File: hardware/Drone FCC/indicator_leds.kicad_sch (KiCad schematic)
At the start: 46 parts, among them Q2 2N7002, Q3 2N7002, Q4 2N7002, Q5 2N7002, Q6 2N7002, Q7 2N7002, Q8 2N7002, Q9 2N7002, SW2 SW_MEC_5E, SW3 SW_MEC_5E

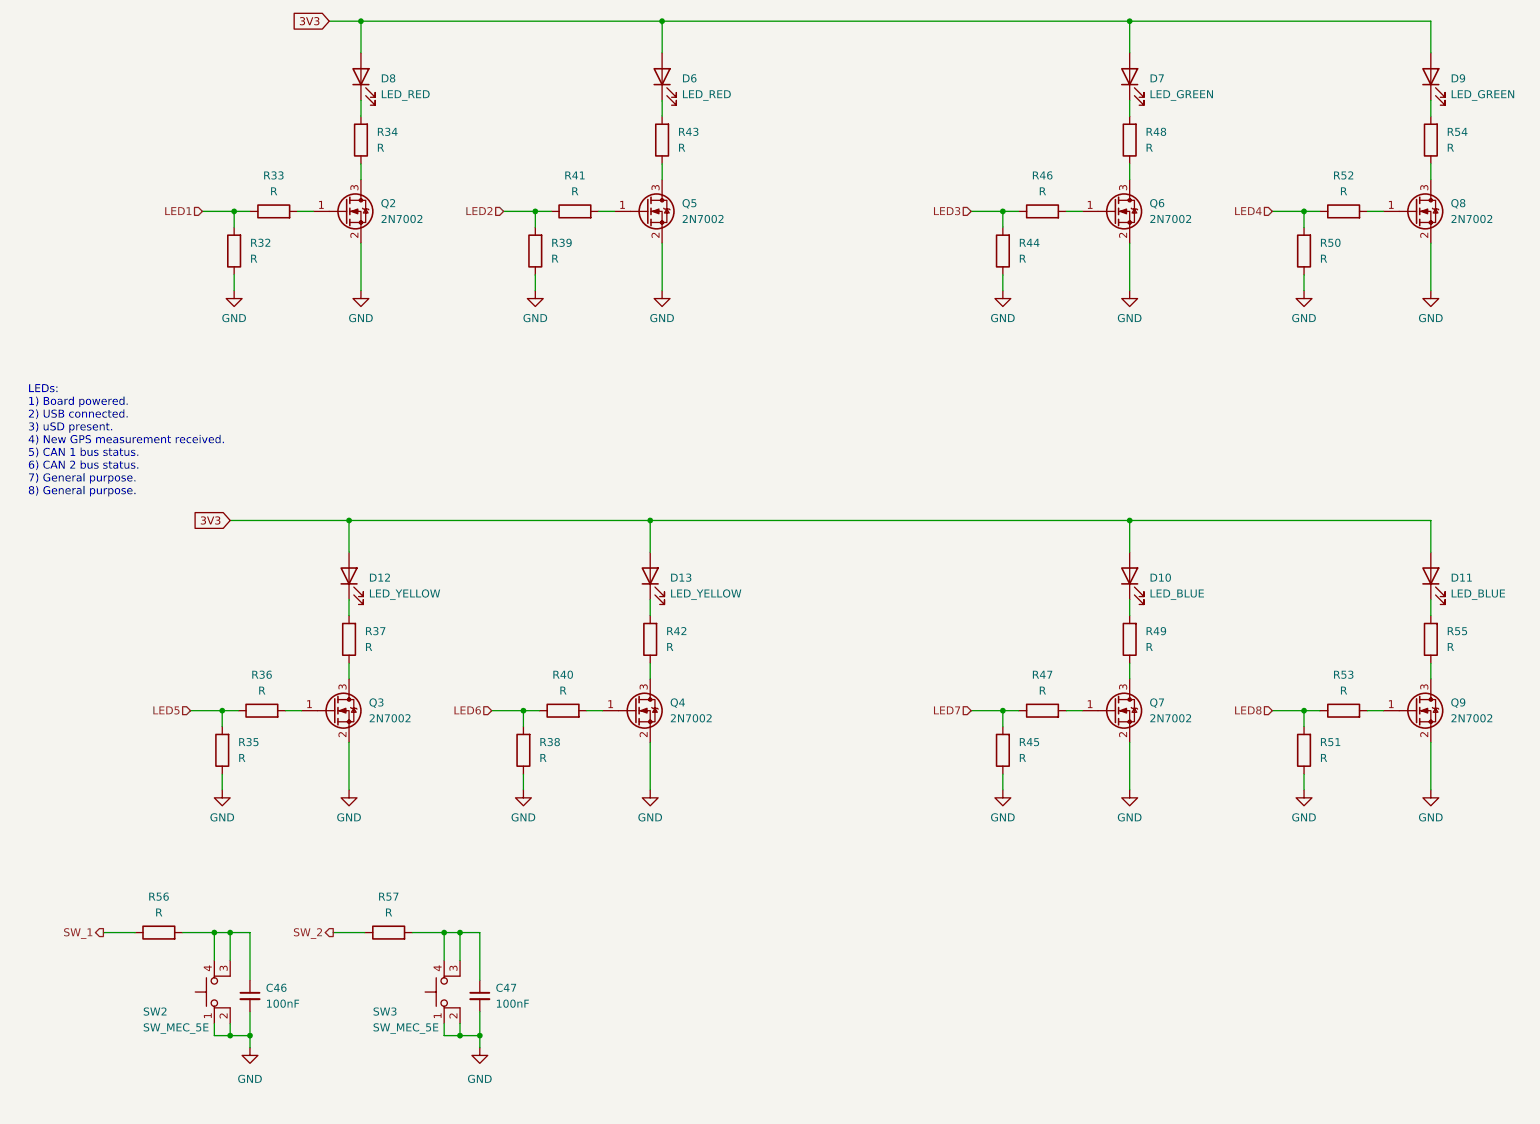
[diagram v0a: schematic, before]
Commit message: re enumeration of components
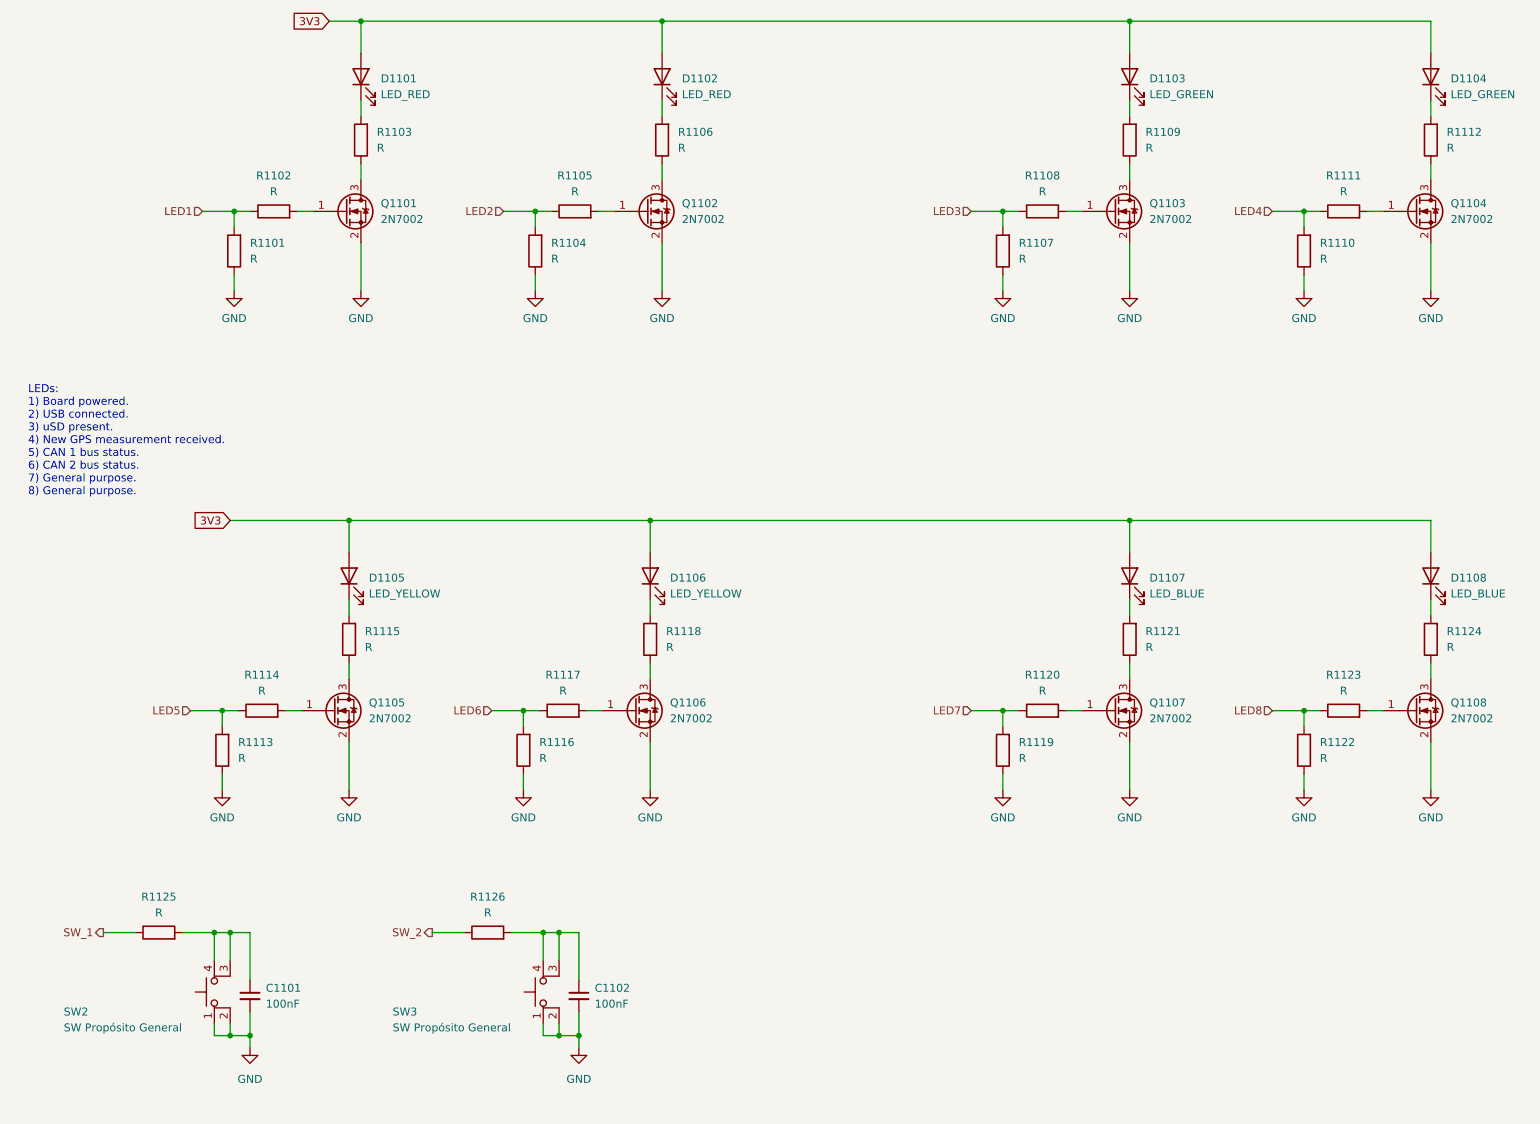
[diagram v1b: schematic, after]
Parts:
- SW2, SW3: value SW_MEC_5E -> SW Propósito General
- renumbered C46 to C1101, C47 to C1102, D8 to D1101, D6 to D1102, D7 to D1103, D9 to D1104, D12 to D1105, D13 to D1106, D10 to D1107, D11 to D1108, Q2 to Q1101, Q5 to Q1102, Q6 to Q1103, Q8 to Q1104, Q3 to Q1105, Q4 to Q1106, Q7 to Q1107, Q9 to Q1108, R32 to R1101, R33 to R1102, R34 to R1103, R39 to R1104, R41 to R1105, R43 to R1106, R44 to R1107, R46 to R1108, R48 to R1109, R50 to R1110, R52 to R1111, R54 to R1112, R35 to R1113, R36 to R1114, R37 to R1115, R38 to R1116, R40 to R1117, R42 to R1118, R45 to R1119, R47 to R1120, R49 to R1121, R51 to R1122, R53 to R1123, R55 to R1124, R56 to R1125, R57 to R1126
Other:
- moved on the sheet: C1102, R1126, SW3

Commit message: start routing
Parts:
- removed SW2, SW3: SW Propósito General, Button_Switch_SMD:SW_SPST_TL3305A, symbol Switch:SW_MEC_5E
- added SW1101, SW1102: SW Propósito General, Button_Switch_SMD:SW_SPST_TL3305A, symbol Switch:SW_Push
- C1101, C1102: footprint (none) -> Capacitor_SMD:C_0402_1005Metric_Pad0.74x0.62mm_HandSolder
- R1101, R1102, R1104, R1105, R1107, R1108, R1110, R1111, R1113, R1114, R1116, R1117, R1119, R1120, R1122, R1123, R1125, R1126: footprint (none) -> Resistor_SMD:R_0402_1005Metric_Pad0.72x0.64mm_HandSolder
- R1103, R1106, R1109, R1112, R1115, R1118, R1121, R1124: footprint (none) -> Resistor_SMD:R_0805_2012Metric_Pad1.20x1.40mm_HandSolder
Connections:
- net GND: now also SW1101.1, SW1102.1
- net at C1102.1, R1126.2: now also SW1102.2
- net at C1101.1, R1125.2: now also SW1101.2

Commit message: add 3D models to footprints
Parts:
- removed SW1101, SW1102: SW Propósito General, Button_Switch_SMD:SW_SPST_TL3305A, symbol Switch:SW_Push
- added SW1101, SW1102: SW Proposito General, TL3305AF160QG:SW_TL3305AF160QG, symbol Switch:SW_MEC_5E
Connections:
- net GND: now also SW1101.1, SW1101.2, SW1102.1, SW1102.2
- net at C1102.1, R1126.2: now also SW1102.3 (K), SW1102.4 (A)
- net at C1101.1, R1125.2: now also SW1101.3 (K), SW1101.4 (A)
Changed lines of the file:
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@@
   (junction (at 49.53 47.625) (diameter 0) (color 0 0 0 0)
   )
+  (junction (at 99.06 165.735) (diameter 0) (color 0 0 0 0)
+  )
   (junction (at 46.355 163.195) (diameter 0) (color 0 0 0 0)
   )
@@
   (junction (at 99.06 163.195) (diameter 0) (color 0 0 0 0)
   )
+  (junction (at 46.355 165.735) (diameter 0) (color 0 0 0 0)
+  )
+  (junction (at 46.355 179.705) (diameter 0) (color 0 0 0 0)
+  )
   (junction (at 220.98 47.625) (diameter 0) (color 0 0 0 0)
   )
@@
   (junction (at 67.945 97.155) (diameter 0) (color 0 0 0 0)
   )
+  (junction (at 99.06 179.705) (diameter 0) (color 0 0 0 0)
+  )
   (junction (at 172.72 127.635) (diameter 0) (color 0 0 0 0)
   )
@@
     (stroke (width 0) (type default) (color 0 0 0 0))
   )
+  (wire (pts (xy 96.52 179.705) (xy 99.06 179.705))
+    (stroke (width 0) (type default) (color 0 0 0 0))
+  )
   (wire (pts (xy 182.88 47.625) (xy 185.42 47.625))
     (stroke (width 0) (type default) (color 0 0 0 0))
@@
     (stroke (width 0) (type default) (color 0 0 0 0))
   )
+  (wire (pts (xy 96.52 177.8) (xy 96.52 179.705))
+    (stroke (width 0) (type default) (color 0 0 0 0))
+  )
   (wire (pts (xy 193.04 17.145) (xy 193.04 22.225))
     (stroke (width 0) (type default) (color 0 0 0 0))
@@
     (stroke (width 0) (type default) (color 0 0 0 0))
   )
+  (wire (pts (xy 43.815 165.735) (xy 46.355 165.735))
+    (stroke (width 0) (type default) (color 0 0 0 0))
+  )
+  (wire (pts (xy 99.06 163.195) (xy 99.06 165.735))
+    (stroke (width 0) (type default) (color 0 0 0 0))
+  )
   (wire (pts (xy 67.945 97.155) (xy 67.945 102.235))
     (stroke (width 0) (type default) (color 0 0 0 0))
@@
     (stroke (width 0) (type default) (color 0 0 0 0))
   )
+  (wire (pts (xy 46.355 165.735) (xy 46.355 167.64))
+    (stroke (width 0) (type default) (color 0 0 0 0))
+  )
   (wire (pts (xy 57.785 127.635) (xy 60.325 127.635))
     (stroke (width 0) (type default) (color 0 0 0 0))
@@
     (stroke (width 0) (type default) (color 0 0 0 0))
   )
+  (wire (pts (xy 43.815 177.8) (xy 43.815 179.705))
+    (stroke (width 0) (type default) (color 0 0 0 0))
+  )
   (wire (pts (xy 116.205 132.715) (xy 116.205 140.335))
     (stroke (width 0) (type default) (color 0 0 0 0))
@@
     (stroke (width 0) (type default) (color 0 0 0 0))
   )
+  (wire (pts (xy 96.52 167.64) (xy 96.52 165.735))
+    (stroke (width 0) (type default) (color 0 0 0 0))
+  )
   (wire (pts (xy 67.945 120.015) (xy 67.945 122.555))
     (stroke (width 0) (type default) (color 0 0 0 0))
@@
     (stroke (width 0) (type default) (color 0 0 0 0))
   )
+  (wire (pts (xy 96.52 165.735) (xy 99.06 165.735))
+    (stroke (width 0) (type default) (color 0 0 0 0))
+  )
   (wire (pts (xy 118.11 40.005) (xy 118.11 42.545))
     (stroke (width 0) (type default) (color 0 0 0 0))
@@
     (stroke (width 0) (type default) (color 0 0 0 0))
   )
+  (wire (pts (xy 43.815 167.64) (xy 43.815 165.735))
+    (stroke (width 0) (type default) (color 0 0 0 0))
+  )
   (wire (pts (xy 167.64 127.635) (xy 172.72 127.635))
     (stroke (width 0) (type default) (color 0 0 0 0))
@@
     (stroke (width 0) (type default) (color 0 0 0 0))
   )
+  (wire (pts (xy 43.815 179.705) (xy 46.355 179.705))
+    (stroke (width 0) (type default) (color 0 0 0 0))
+  )
   (wire (pts (xy 118.11 52.705) (xy 118.11 60.325))
     (stroke (width 0) (type default) (color 0 0 0 0))
@@
     (stroke (width 0) (type default) (color 0 0 0 0))
   )
+  (wire (pts (xy 99.06 165.735) (xy 99.06 167.64))
+    (stroke (width 0) (type default) (color 0 0 0 0))
+  )
   (wire (pts (xy 52.07 175.895) (xy 52.07 179.705))
     (stroke (width 0) (type default) (color 0 0 0 0))
@@
     (stroke (width 0) (type default) (color 0 0 0 0))
   )
-  (wire (pts (xy 46.355 163.195) (xy 46.355 167.64))
+  (wire (pts (xy 46.355 163.195) (xy 46.355 165.735))
     (stroke (width 0) (type default) (color 0 0 0 0))
   )
@@
   )
   (wire (pts (xy 241.3 109.855) (xy 241.3 112.395))
-    (stroke (width 0) (type default) (color 0 0 0 0))
-  )
-  (wire (pts (xy 99.06 163.195) (xy 99.06 167.64))
     (stroke (width 0) (type default) (color 0 0 0 0))
   )
@@
     (pin "2")
   )
-  (symbol (lib_id "Switch:SW_Push") (at 46.355 172.72 90) (unit 1)
-    (in_bom yes) (on_board yes)
-    (property "Reference" "SW1101" (id 0) (at 34.925 171.45 90)
-      (effects (font (size 1.27 1.27)) (justify right))
-    )
-    (property "Value" "SW Propósito General" (id 1) (at 21.59 173.99 90)
-      (effects (font (size 1.27 1.27)) (justify right))
-    )
-    (property "Footprint" "Button_Switch_SMD:SW_SPST_TL3305A" (id 2) (at 41.275 172.72 0)
-      (effects (font (size 1.27 1.27)) hide)
-    )
-    (property "Datasheet" "~" (id 3) (at 41.275 172.72 0)
-      (effects (font (size 1.27 1.27)) hide)
-    )
-    (pin "1")
-    (pin "2")
-  )
   (symbol (lib_id "Device:R") (at 241.3 36.195 180) (unit 1)
     (in_bom yes) (on_board yes) (fields_autoplaced)
@@
     (pin "1")
   )
+  (symbol (lib_id "Switch:SW_MEC_5E") (at 46.355 172.72 90) (unit 1)
+    (in_bom yes) (on_board yes)
+    (property "Reference" "SW1101" (id 0) (at 32.385 172.085 90)
+      (effects (font (size 1.27 1.27)) (justify right))
+    )
+    (property "Value" "SW Proposito General" (id 1) (at 19.05 174.625 90)
+      (effects (font (size 1.27 1.27)) (justify right))
+    )
+    (property "Footprint" "TL3305AF160QG:SW_TL3305AF160QG" (id 2) (at 38.735 172.72 0)
+      (effects (font (size 1.27 1.27)) hide)
+    )
+    (property "Datasheet" "http://www.apem.com/int/index.php?controller=attachment&id_attachment=1371" (id 3) (at 38.735 172.72 0)
+      (effects (font (size 1.27 1.27)) hide)
+    )
+    (pin "1")
+    (pin "2")
+    (pin "3")
+    (pin "4")
+  )
   (symbol (lib_id "Device:R") (at 220.98 53.975 180) (unit 1)
     (in_bom yes) (on_board yes) (fields_autoplaced)
@@
     (pin "1")
   )
-  (symbol (lib_id "Switch:SW_Push") (at 99.06 172.72 90) (unit 1)
-    (in_bom yes) (on_board yes)
-    (property "Reference" "SW1102" (id 0) (at 87.63 171.45 90)
-      (effects (font (size 1.27 1.27)) (justify right))
-    )
-    (property "Value" "SW Propósito General" (id 1) (at 74.295 173.99 90)
-      (effects (font (size 1.27 1.27)) (justify right))
-    )
-    (property "Footprint" "Button_Switch_SMD:SW_SPST_TL3305A" (id 2) (at 93.98 172.72 0)
-      (effects (font (size 1.27 1.27)) hide)
-    )
-    (property "Datasheet" "~" (id 3) (at 93.98 172.72 0)
-      (effects (font (size 1.27 1.27)) hide)
-    )
-    (pin "1")
-    (pin "2")
-  )
   (symbol (lib_id "Device:R") (at 193.04 36.195 180) (unit 1)
     (in_bom yes) (on_board yes) (fields_autoplaced)
@@
     (pin "1")
   )
+  (symbol (lib_id "Switch:SW_MEC_5E") (at 99.06 172.72 90) (unit 1)
+    (in_bom yes) (on_board yes)
+    (property "Reference" "SW1102" (id 0) (at 85.09 172.085 90)
+      (effects (font (size 1.27 1.27)) (justify right))
+    )
+    (property "Value" "SW Proposito General" (id 1) (at 71.755 174.625 90)
+      (effects (font (size 1.27 1.27)) (justify right))
+    )
+    (property "Footprint" "TL3305AF160QG:SW_TL3305AF160QG" (id 2) (at 91.44 172.72 0)
+      (effects (font (size 1.27 1.27)) hide)
+    )
+    (property "Datasheet" "http://www.apem.com/int/index.php?controller=attachment&id_attachment=1371" (id 3) (at 91.44 172.72 0)
+      (effects (font (size 1.27 1.27)) hide)
+    )
+    (pin "1")
+    (pin "2")
+    (pin "3")
+    (pin "4")
+  )
   (symbol (lib_id "Device:R") (at 227.33 47.625 90) (unit 1)

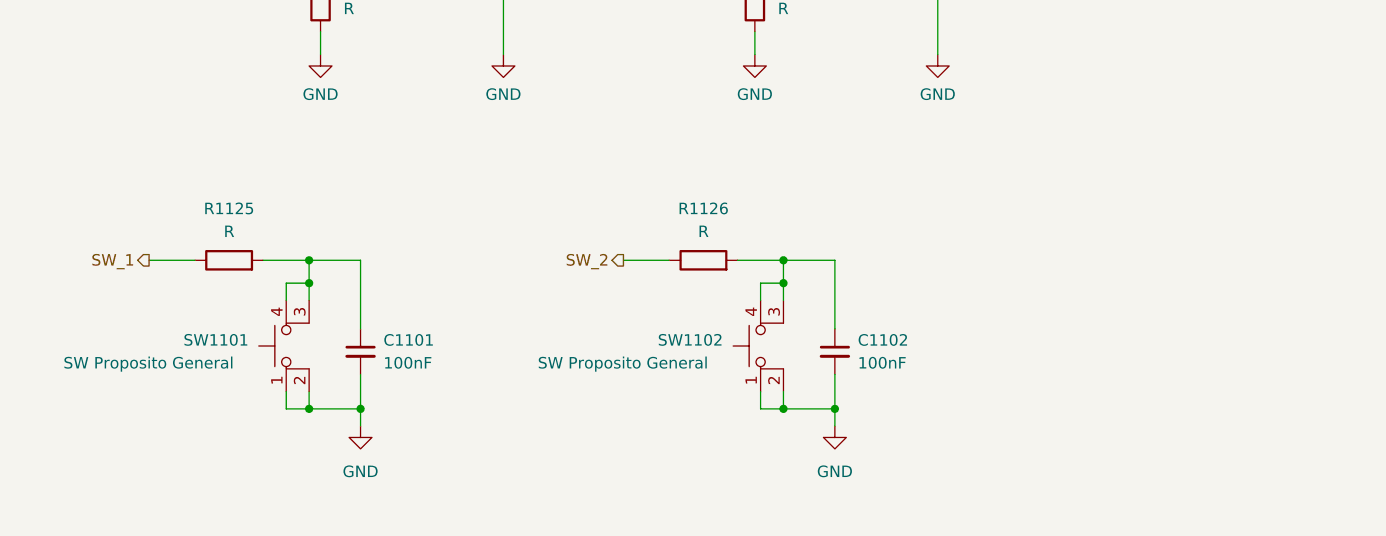
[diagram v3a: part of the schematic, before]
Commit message: added missing TVS diodes
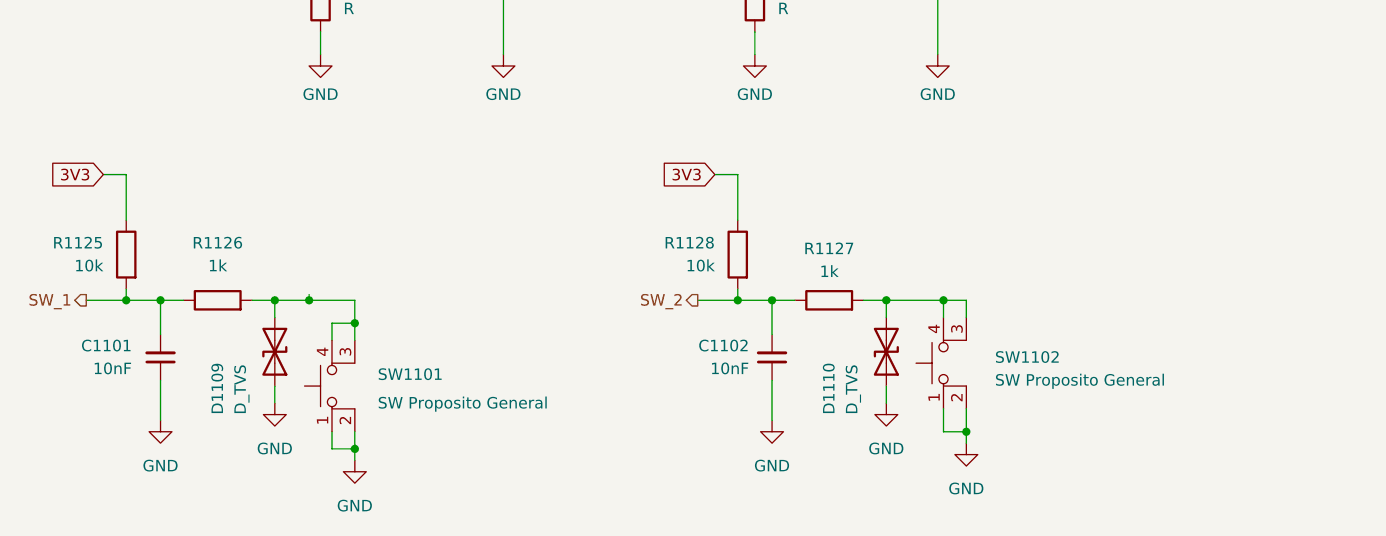
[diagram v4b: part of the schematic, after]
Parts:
- added D1109, D1110: D_TVS, Diode_SMD:D_0402_1005Metric_Pad0.77x0.64mm_HandSolder, symbol Device:D_TVS
- added R1127: 1k, Resistor_SMD:R_0402_1005Metric_Pad0.72x0.64mm_HandSolder, symbol Device:R
- added R1128: 10k, Resistor_SMD:R_0402_1005Metric_Pad0.72x0.64mm_HandSolder, symbol Device:R
- C1101, C1102: value 100nF -> 10nF
- R1125: value R -> 10k
- R1126: value R -> 1k
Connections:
- net 3V3: now also R1125.1, R1128.1
- net GND: now also C1101.1, C1102.1, D1109.1 (A1), D1110.1 (A1); no longer C1101.2, C1102.2
- net SW_1: now also C1101.2, R1125.2, R1126.1; no longer R1125.1
- net SW_2: now also C1102.2, R1127.1, R1128.2; no longer R1126.1
- net at SW1102.3 (K), SW1102.4 (A): now also D1110.2 (A2), R1127.2; no longer C1102.1, R1126.2
- net at SW1101.3 (K), SW1101.4 (A): now also R1126.2, D1109.2 (A2); no longer C1101.1, R1125.2
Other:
- moved on the sheet: SW1101, SW1102
